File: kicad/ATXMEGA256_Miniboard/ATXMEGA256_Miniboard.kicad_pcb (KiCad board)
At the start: 4 copper layers, 55 x 102 mm, 49 parts, among them J1 10118192-0001LF, J10 2x5 Goldpin Socket, J11 2x5 Goldpin Socket, J12 2x5 Goldpin Socket, J13 2x5 Goldpin Socket, J14 2x5 Goldpin Socket, J15 2x5 Goldpin Socket, J2 2x5 IDC Socket, J3 2x3 IDC Socket, J4 1x3 Goldpin Header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

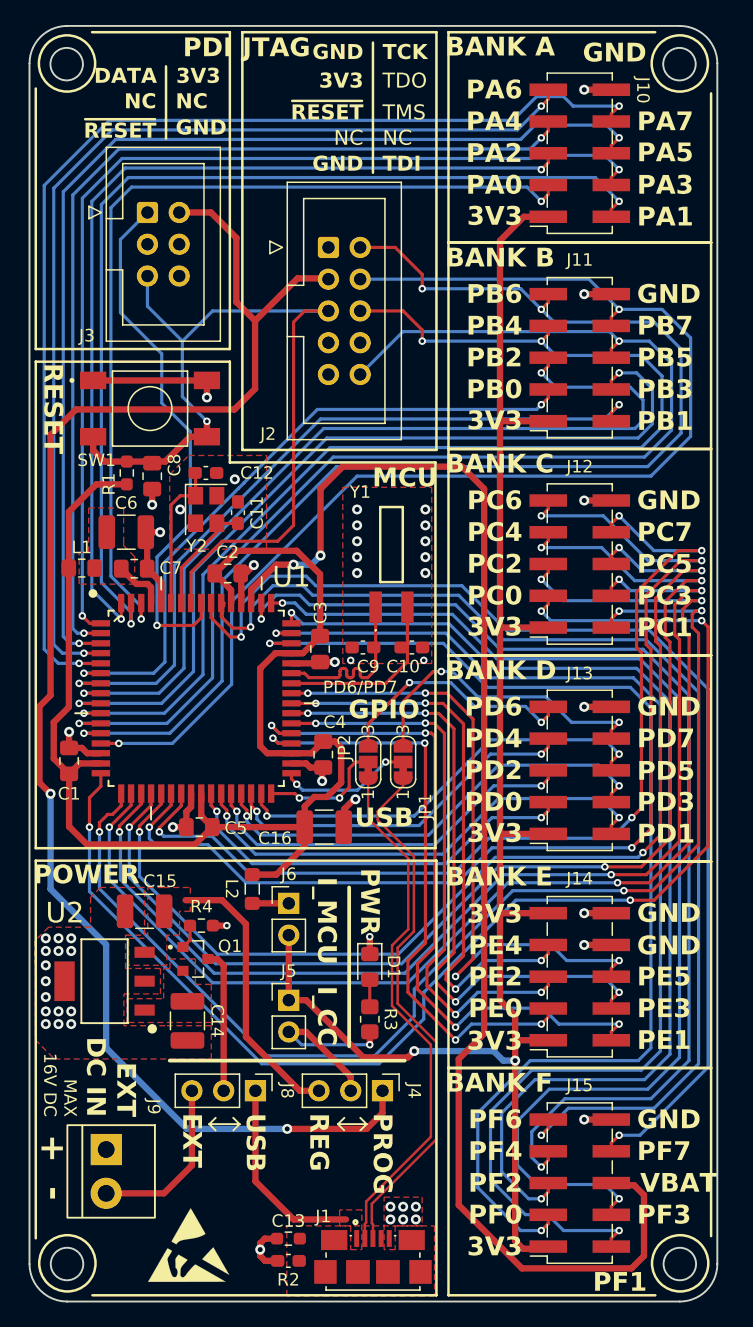
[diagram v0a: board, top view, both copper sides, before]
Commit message: update BOM, poprawki masy
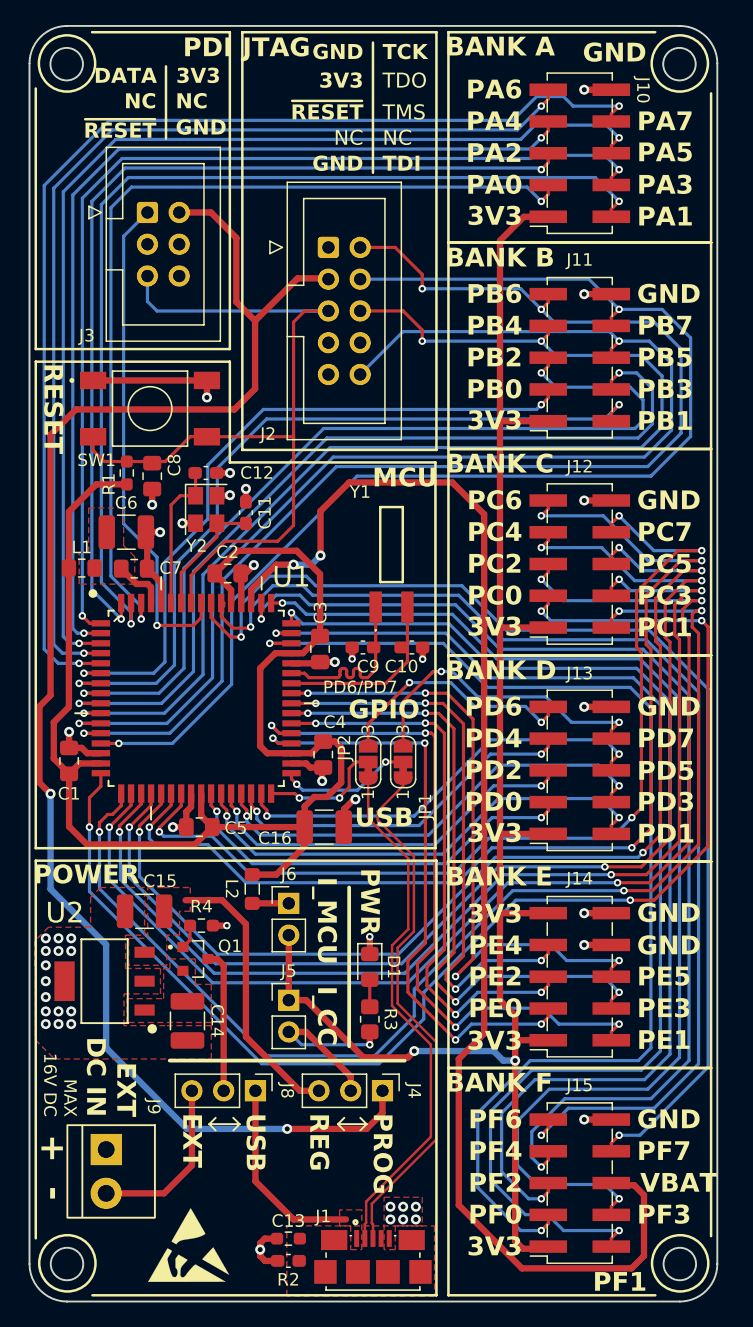
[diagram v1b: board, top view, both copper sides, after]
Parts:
- moved C11 0.63 mm to (185.2, 76.1)
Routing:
- net GND: track 62.3 -> 68.4 mm, vias 54 -> 46
- net /~{RESET}: track 70.5 -> 66.6 mm, vias 1 -> 0
- net /VBAT: track 110.9 -> 107.6 mm
- net /PB1: track 60.4 -> 62.9 mm
- net /PB0: track 53.0 -> 55.5 mm
- net /PDI_DATA: track 42.3 -> 39.9 mm
- net Net-(U1-PR0): track 9.25 -> 9.89 mm
